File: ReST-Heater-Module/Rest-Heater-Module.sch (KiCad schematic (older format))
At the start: 14 parts, among them P1 02X10-MALE, P3 02-SCREW-TERM, P4 01X02-MALE, P5 02-SCREW-TERM, Q1 Q_BSH105, Q2 Q_AOT240L

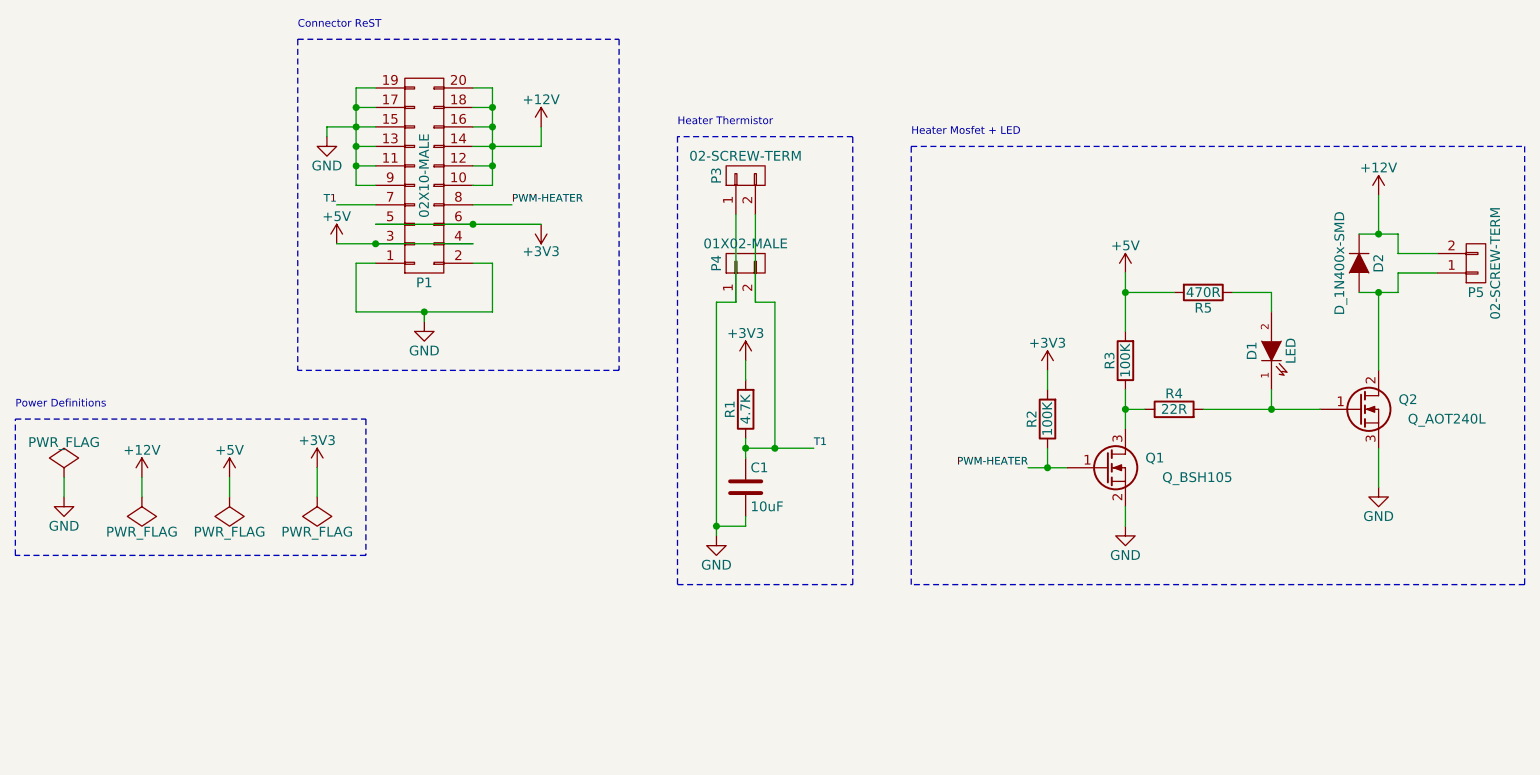
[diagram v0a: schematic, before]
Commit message: PRE-RELEASE Rev. A!
Yay. I managed to finish the Main PCB over the night, must say, Im happy with it. Things that changed since the last release:

Heater:
-Heater Module uses less Pins
- Much smaller Design now

Heatbed & Additional Module: 
-Changed distance from Edge to first Pin from 2.5mm to 2mm (will be changed on other boards too)

Mainboard:
-Added I2C Pullups 4K7
-Swapped Pins from Stepper, Heaters and Endstops around for easier PCB Design.
-Finished Design (10cm x 10cm!)

Added some 3D Models for testing. If someone has problems with loading some modules, please contact me! (or make a pull request with a better solution)
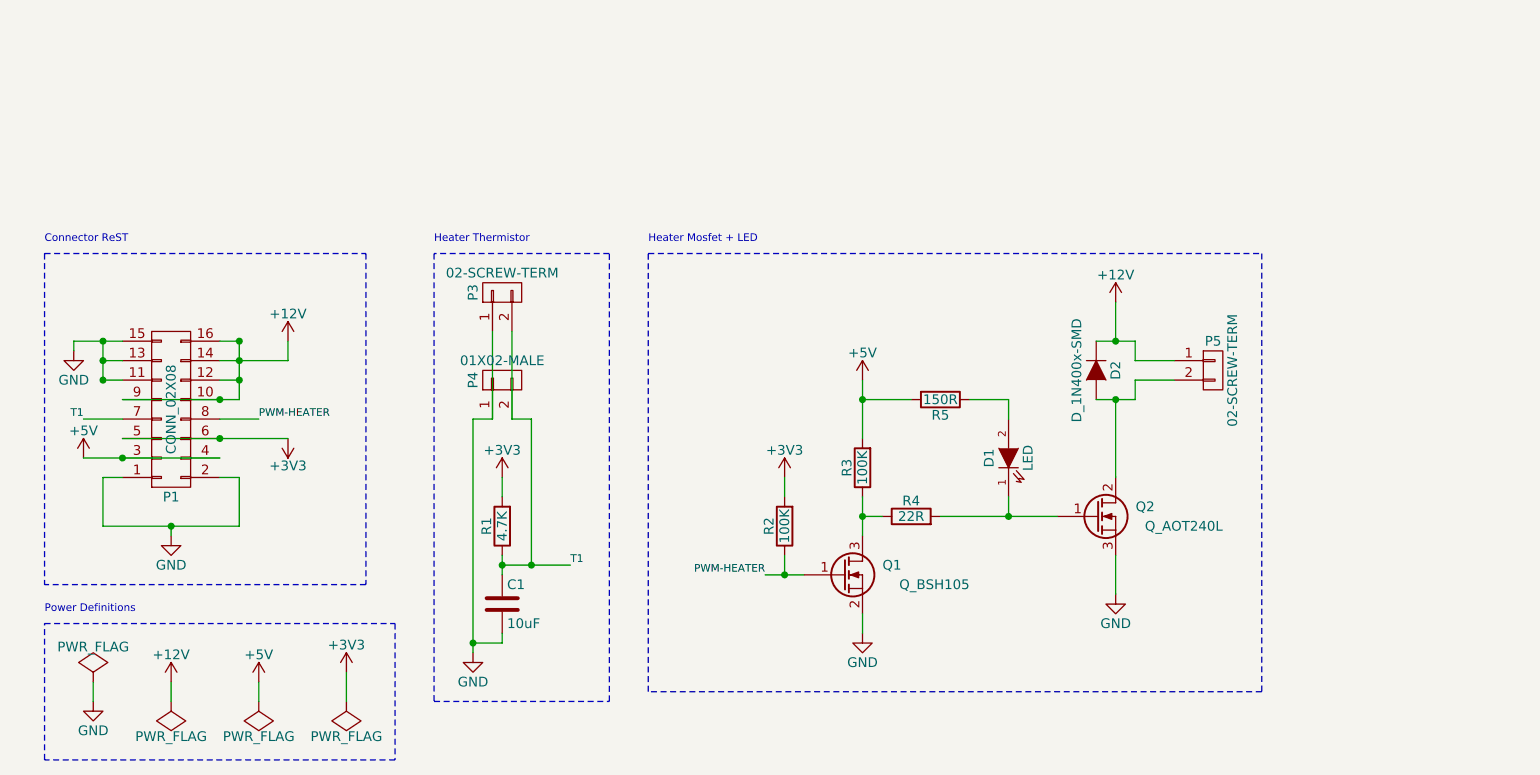
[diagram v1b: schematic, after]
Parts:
- removed P1: 02X10-MALE, Pin_Headers:Pin_Header_Angled_2x10, symbol CONN_02X10
- added P1: CONN_02X08, Pin_Headers:Pin_Header_Angled_2x08, symbol CONN_02X08
- C1: footprint ok-smd-generic:1206 -> Capacitors_SMD:C_0805_HandSoldering
- D2: footprint DO-214AC(SMA):DO-214AC(SMA) -> ReST-Library:DO-214AC(SMA)
- P3: footprint 2:mpt_0,5%2f2-2,54 -> ReST-Library:screw-2,54-2P
- P5: footprint 5mm-pitch-terminal:mkds_1,5-2 -> ReST-Library:screw-5-2P
- R1, R2, R3, R4: footprint ok-smd-generic:1206 -> Resistors_SMD:R_0805_HandSoldering
- R5: value 470R -> 150R; footprint ok-smd-generic:1206 -> Resistors_SMD:R_0805_HandSoldering
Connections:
- net +12V: now also P5.1 (P1), P1.10 (P10), P1.12 (P12), P1.14 (P14), P1.16 (P16), P1.9 (P9); no longer P5.2 (P2)
- net +3V3: now also P1.5 (P5), P1.6 (P6)
- net +5V: now also P1.3 (P3), P1.4 (P4)
- net GND: now also P1.1 (P1), P1.11 (P11), P1.13 (P13), P1.15 (P15), P1.2 (P2)
- net PWM-HEATER: now also P1.8 (P8)
- net T1: now also P1.7 (P7)
- net at D2.2 (A), Q2.2 (D): now also P5.2 (P2); no longer P5.1 (P1)
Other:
- moved on the sheet: C1, D1, D2, P3, P4, P5, Q1, Q2, R1, R2, R3, R4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

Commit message: Finally removed all unnecessary Libs and added Heatsink for 5V Regulator
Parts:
- Q1: footprint TO_SOT_Packages_SMD:SOT-23 -> ReST-Library:SOT-23
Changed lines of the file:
@@
 LIBS:dc-dc
 LIBS:diode
-LIBS:dp_devices
 LIBS:elec-unifil
 LIBS:ESD_Protection
@@
 LIBS:nordicsemi
 LIBS:nxp_armmcu
-LIBS:ok-74logic
-LIBS:ok-con-generic
-LIBS:ok-diodes
-LIBS:ok-generic
-LIBS:ok-ic-analog
-LIBS:ok-ic-atmel
-LIBS:ok-ic-com
-LIBS:ok-ic-memory
-LIBS:ok-ic-power
-LIBS:ok-ic-special
-LIBS:ok-ic-stm32
-LIBS:ok-jacks
-LIBS:ok-opto
-LIBS:ok-power
-LIBS:ok-relay
-LIBS:ok-switches
-LIBS:ok-transformers
-LIBS:ok-transistors
 LIBS:onsemi
 LIBS:Oscillators
-LIBS:pololu_a4988
 LIBS:Power_Management
 LIBS:powerint
@@
 F 0 "Q1" H 7200 4450 50  0000 R CNN
 F 1 "Q_BSH105" H 7550 4350 50  0000 R CNN
-F 2 "TO_SOT_Packages_SMD:SOT-23" H 7100 4500 50  0001 C CNN
+F 2 "ReST-Library:SOT-23" H 7100 4500 50  0001 C CNN
 F 3 "" H 6900 4400 50  0000 C CNN
 	1    6900 4400

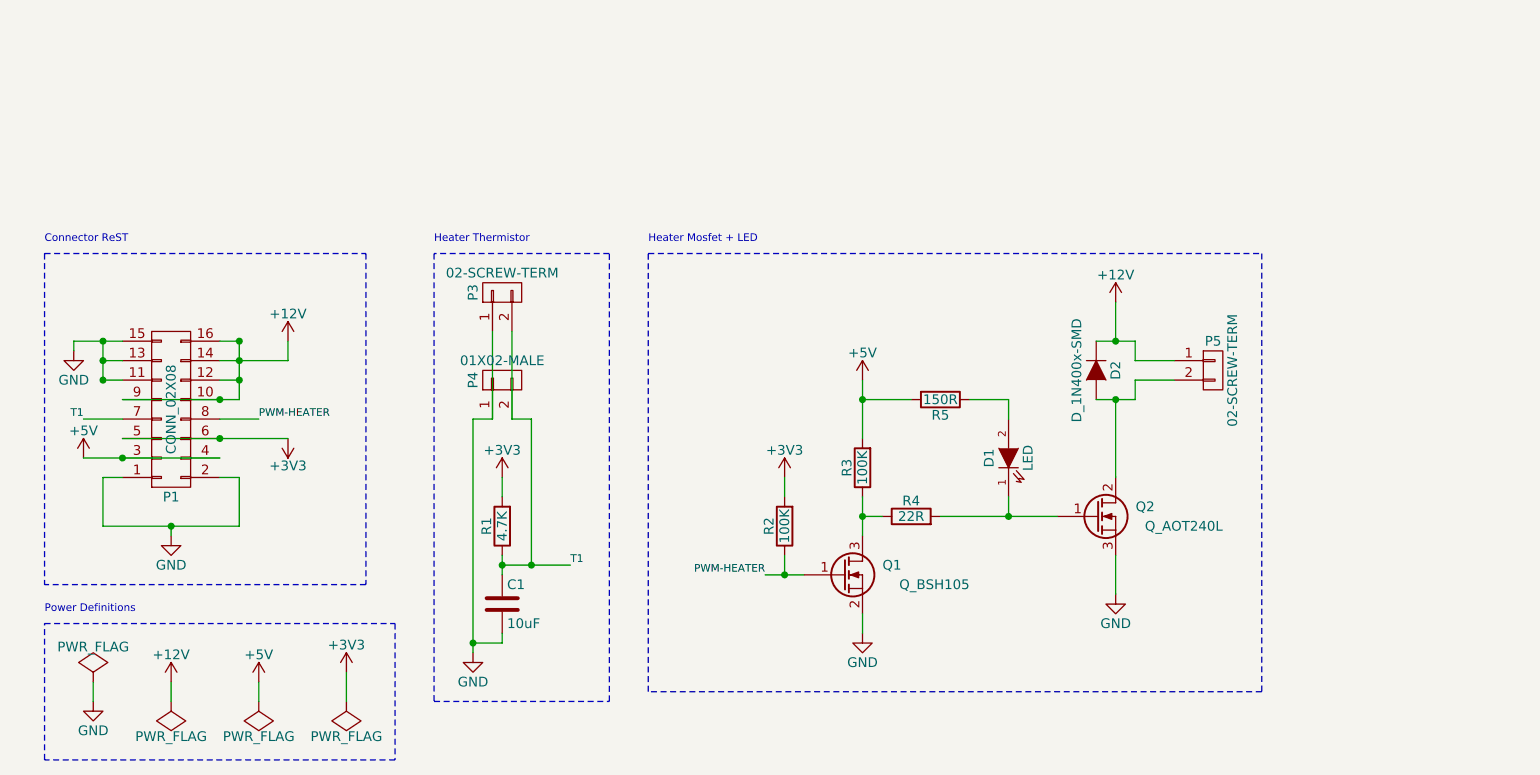
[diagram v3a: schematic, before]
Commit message: Reworked Modules to sit ontop of the mainboard
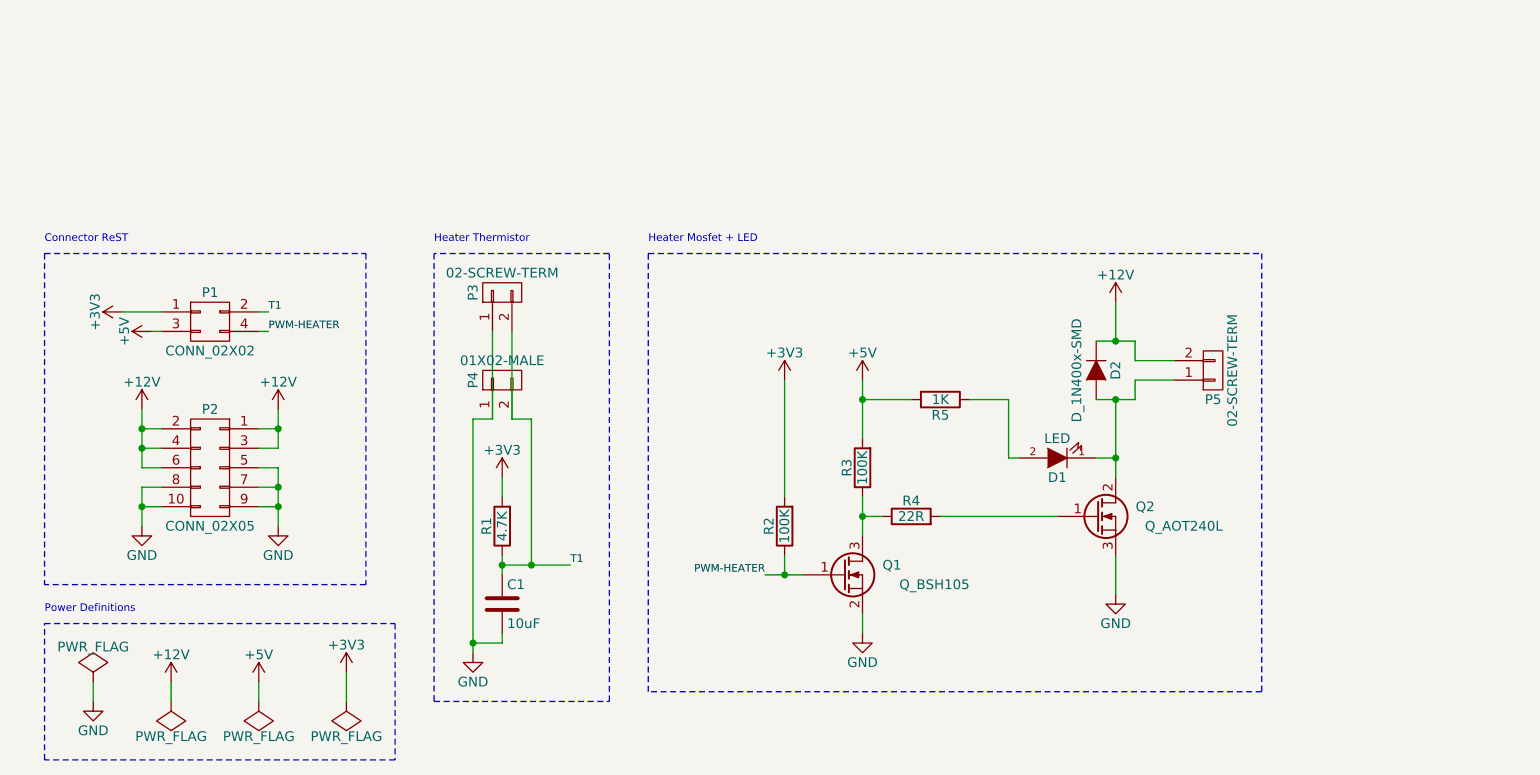
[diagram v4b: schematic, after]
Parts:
- removed P1: CONN_02X08, Pin_Headers:Pin_Header_Angled_2x08, symbol CONN_02X08
- added P1: CONN_02X02, ReST-Library:bb02-hp04, symbol CONN_02X02
- added P2: CONN_02X05, ReST-Library:bb02-hp10, symbol CONN_02X05
- D2: footprint ReST-Library:DO-214AC(SMA) -> ReST-Library:DO-214AC.SMA
- P3: footprint ReST-Library:screw-2,54-2P -> ReST-Library:screw-2.54-2P
- R5: value 150R -> 1K
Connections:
- net +12V: now also P5.2 (P2), P2.1 (P1), P2.2 (P2), P2.3 (P3), P2.4 (P4), P2.6 (P6); no longer P5.1 (P1)
- net +3V3: now also P1.1 (P1)
- net +5V: now also P1.3 (P3)
- net GND: now also P2.10 (P10), P2.5 (P5), P2.7 (P7), P2.8 (P8), P2.9 (P9)
- net PWM-HEATER: now also P1.4 (P4)
- net T1: now also P1.2 (P2)
- net at Q2.1 (G), R4.2: no longer D1.1 (K)
- net at D2.2 (A), Q2.2 (D): now also D1.1 (K), P5.1 (P1); no longer P5.2 (P2)
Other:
- moved on the sheet: D1

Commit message: Changes in Heatbed and Heater + F1 and F4 Pinout table with functions
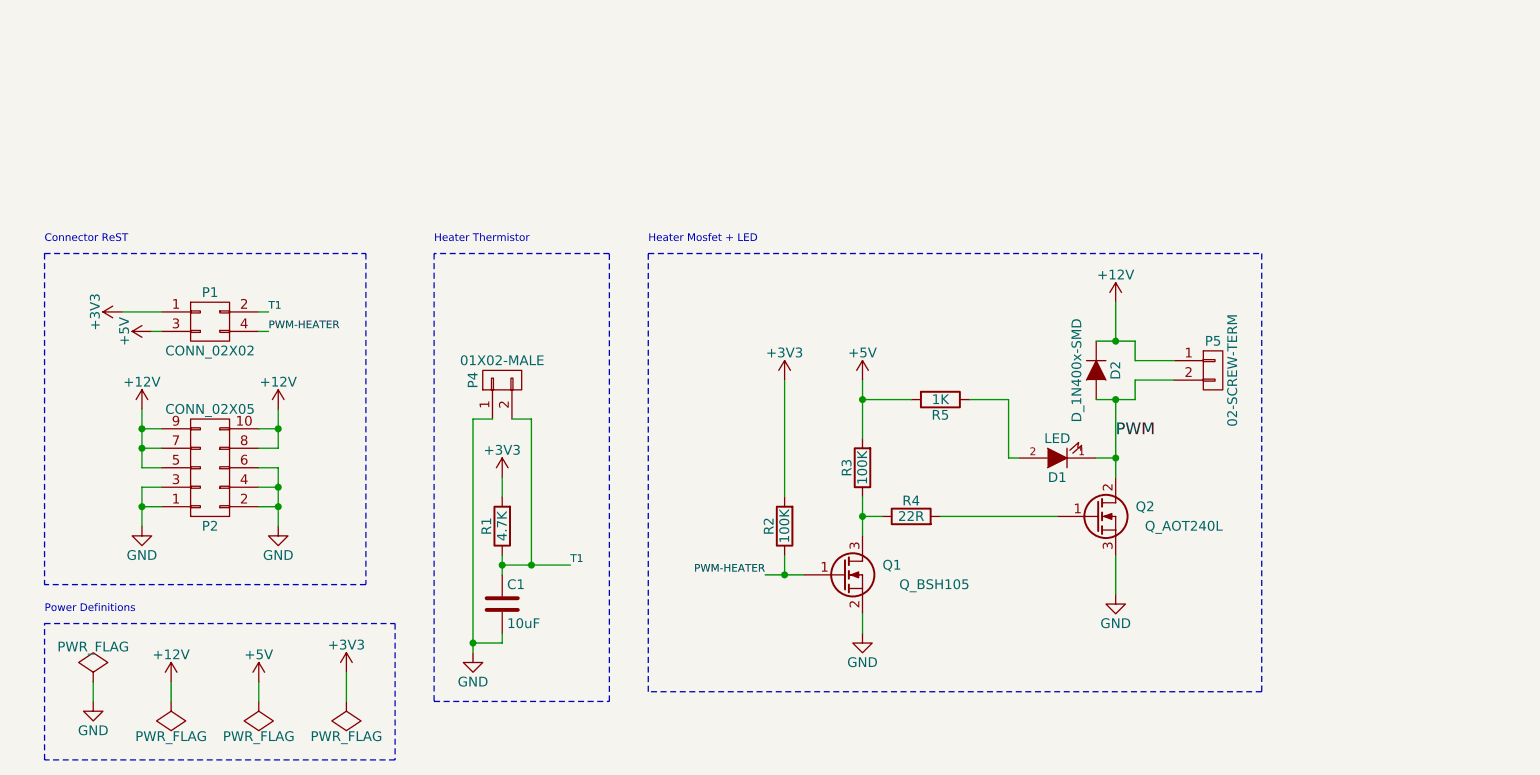
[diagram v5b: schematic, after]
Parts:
- removed P3: 02-SCREW-TERM, ReST-Library:screw-2.54-2P, symbol CONN_01X02
- P4: footprint Pin_Headers:Pin_Header_Straight_1x02 -> ReST-Library:bb02-hy02a
- R1, R2, R3, R4, R5: footprint Resistors_SMD:R_0805_HandSoldering -> Resistors_SMD:R_0603_HandSoldering
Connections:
- net +12V: now also P2.10 (P10), P2.5 (P5), P2.7 (P7), P2.8 (P8), P2.9 (P9), P5.1 (P1); no longer P2.1 (P1), P2.2 (P2), P2.3 (P3), P2.4 (P4), P2.6 (P6), P5.2 (P2)
- net GND: now also P2.1 (P1), P2.2 (P2), P2.3 (P3), P2.4 (P4), P2.6 (P6); no longer P2.10 (P10), P2.5 (P5), P2.7 (P7), P2.8 (P8), P2.9 (P9)
- net PWM: now reaches D1.1 (K), D2.2 (A), Q2.2 (D)
- net PWM: now also P5.2 (P2); no longer P5.1 (P1)
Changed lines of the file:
@@
 F 3 "" H 8800 3350 50  0000 C CNN
 	1    8800 3350
-	1    0    0    1
+	1    0    0    -1
 $EndComp
 $Comp
@@
 F 0 "R4" V 7330 4100 50  0000 C CNN
 F 1 "22R" V 7250 4100 50  0000 C CNN
-F 2 "Resistors_SMD:R_0805_HandSoldering" V 7180 4100 50  0001 C CNN
+F 2 "Resistors_SMD:R_0603_HandSoldering" V 7180 4100 50  0001 C CNN
 F 3 "" H 7250 4100 50  0000 C CNN
 	1    7250 4100
@@
 $EndComp
 $Comp
-L CONN_01X02 P3
-U 1 1 56A6ACF0
-P 5150 2950
-F 0 "P3" H 5150 3100 50  0000 C CNN
-F 1 "02-SCREW-TERM" V 5250 2950 50  0000 C CNN
-F 2 "ReST-Library:screw-2.54-2P" H 5150 2950 50  0001 C CNN
-F 3 "" H 5150 2950 50  0000 C CNN
-	1    5150 2950
-	0    -1   -1   0
-$EndComp
-$Comp
 L CONN_01X02 P4
 U 1 1 56A6AD1A
@@
 F 0 "P4" H 5150 3550 50  0000 C CNN
 F 1 "01X02-MALE" V 5250 3400 50  0000 C CNN
-F 2 "Pin_Headers:Pin_Header_Straight_1x02" H 5150 3400 50  0001 C CNN
+F 2 "ReST-Library:bb02-hy02a" H 5150 3400 50  0001 C CNN
 F 3 "" H 5150 3400 50  0000 C CNN
 	1    5150 3400
@@
 F 0 "R1" V 5230 4150 50  0000 C CNN
 F 1 "4.7K" V 5150 4150 50  0000 C CNN
-F 2 "Resistors_SMD:R_0805_HandSoldering" V 5080 4150 50  0001 C CNN
+F 2 "Resistors_SMD:R_0603_HandSoldering" V 5080 4150 50  0001 C CNN
 F 3 "" H 5150 4150 50  0000 C CNN
 	1    5150 4150
@@
 F 0 "R2" V 6680 4150 50  0000 C CNN
 F 1 "100K" V 6600 4150 50  0000 C CNN
-F 2 "Resistors_SMD:R_0805_HandSoldering" V 6530 4150 50  0001 C CNN
+F 2 "Resistors_SMD:R_0603_HandSoldering" V 6530 4150 50  0001 C CNN
 F 3 "" H 6600 4150 50  0000 C CNN
 	1    6600 4150
@@
 F 0 "R3" V 7080 3850 50  0000 C CNN
 F 1 "100K" V 7000 3850 50  0000 C CNN
-F 2 "Resistors_SMD:R_0805_HandSoldering" V 6930 3850 50  0001 C CNN
+F 2 "Resistors_SMD:R_0603_HandSoldering" V 6930 3850 50  0001 C CNN
 F 3 "" H 7000 3850 50  0000 C CNN
 	1    7000 3850
@@
 F 0 "R5" V 7480 3500 50  0000 C CNN
 F 1 "1K" V 7400 3500 50  0000 C CNN
-F 2 "Resistors_SMD:R_0805_HandSoldering" V 7330 3500 50  0001 C CNN
+F 2 "Resistors_SMD:R_0603_HandSoldering" V 7330 3500 50  0001 C CNN
 F 3 "" H 7400 3500 50  0000 C CNN
 	1    7400 3500
@@
 F 3 "" H 3650 2650 50  0000 C CNN
 	1    3650 3850
-	-1   0    0    -1
+	1    0    0    1
 $EndComp
 $Comp
@@
 $EndComp
 Wire Wire Line
-	5100 3600 5100 3150
-Wire Wire Line
-	5200 3150 5200 3600
-Wire Wire Line
 	5150 4000 5150 3900
 Wire Wire Line
@@
 	4000 3850 3900 3850
 Connection ~ 4000 3950
+Text Label 8300 3700 0    60   ~ 0
+PWM
 $EndSCHEMATC
